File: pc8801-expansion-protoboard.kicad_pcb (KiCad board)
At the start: 2 copper layers, 219 x 95 mm, 11 parts, among them J1 Solder Side, J2 Parts Side, J3 5V, J4 12V, J5 -12V, J6 GND_1, J7 GND_2, U1 ExpansionEdge

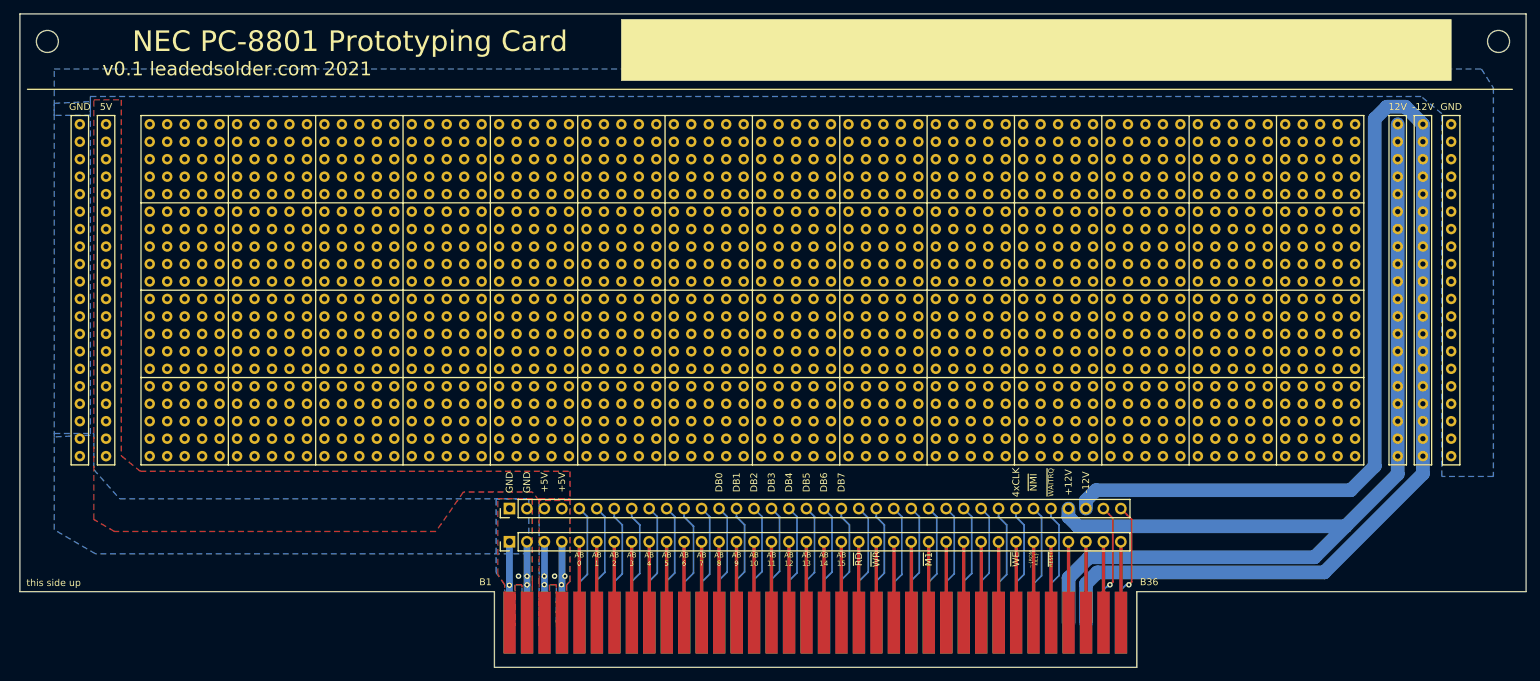
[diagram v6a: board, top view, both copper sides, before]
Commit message: ejector holes
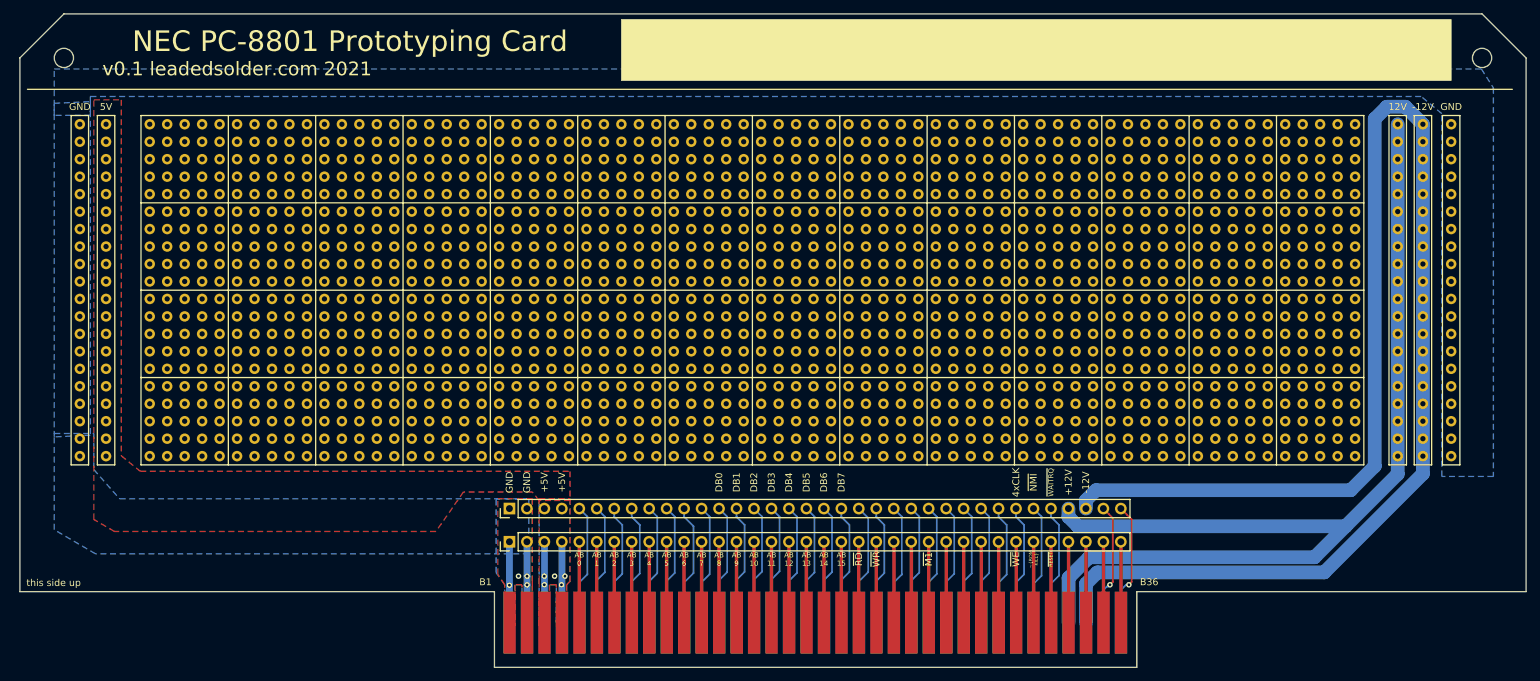
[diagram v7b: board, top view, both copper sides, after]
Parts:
- removed the REF** at (41.0, 54.0)
- removed the REF** at (252.0, 54.0)
- added REF**: MountingHole_2.7mm, MountingHole:MountingHole_2.7mm, F.Cu at (249.6, 56.4)
- added REF**: MountingHole_2.7mm, MountingHole:MountingHole_2.7mm, F.Cu at (43.4, 56.4)
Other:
- outline, holes or cut-outs redrawn
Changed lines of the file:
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@@
   (general
     (thickness 1.6)
-    (drawings 65)
+    (drawings 67)
     (tracks 245)
     (zones 0)
@@
     (38 B.Mask user)
     (39 F.Mask user)
-    (40 Dwgs.User user)
+    (40 Dwgs.User user hide)
     (41 Cmts.User user)
     (42 Eco1.User user)
@@
     (mod_text_size 1 1)
     (mod_text_width 0.15)
-    (pad_size 1.524 1.524)
-    (pad_drill 0.762)
+    (pad_size 2.8 2.8)
+    (pad_drill 2.8)
     (pad_to_mask_clearance 0.051)
     (solder_mask_min_width 0.25)
@@
     (add_net "Net-(J2-Pad9)")
   )
-  (module MountingHole:MountingHole_3.2mm_M3 locked (layer F.Cu)
-    (at 41 54)
-    (descr "Mounting Hole 3.2mm, no annular, M3")
-    (tags "mounting hole 3.2mm no annular m3")
+  (module MountingHole:MountingHole_2.7mm (layer F.Cu)
+    (at 249.6 56.4)
+    (descr "Mounting Hole 2.7mm, no annular")
+    (tags "mounting hole 2.7mm no annular")
     (attr virtual)
-    (fp_text reference REF** (at 0 -4.2) (layer F.SilkS) hide
-      (effects (font (size 1 1) (thickness 0.15)))
-    )
-    (fp_text value MountingHole_3.2mm_M3 (at 0 4.2) (layer F.Fab)
-      (effects (font (size 1 1) (thickness 0.15)))
-    )
-    (fp_circle (center 0 0) (end 3.45 0) (layer F.CrtYd) (width 0.05))
-    (fp_circle (center 0 0) (end 3.2 0) (layer Cmts.User) (width 0.15))
+    (fp_text reference REF** (at 0 -3.7) (layer F.SilkS) hide
+      (effects (font (size 1 1) (thickness 0.15)))
+    )
+    (fp_text value MountingHole_2.7mm (at 0 3.7) (layer F.Fab)
+      (effects (font (size 1 1) (thickness 0.15)))
+    )
+    (fp_circle (center 0 0) (end 2.95 0) (layer F.CrtYd) (width 0.05))
+    (fp_circle (center 0 0) (end 2.7 0) (layer Cmts.User) (width 0.15))
     (fp_text user %R (at 0.3 0) (layer F.Fab)
       (effects (font (size 1 1) (thickness 0.15)))
     )
-    (pad 1 np_thru_hole circle (at 0 0) (size 3.2 3.2) (drill 3.2) (layers *.Cu *.Mask))
-  )
-  (module MountingHole:MountingHole_3.2mm_M3 locked (layer F.Cu)
-    (at 252 54)
-    (descr "Mounting Hole 3.2mm, no annular, M3")
-    (tags "mounting hole 3.2mm no annular m3")
+    (pad "" np_thru_hole circle (at 0 0) (size 2.8 2.8) (drill 2.8) (layers *.Cu *.Mask))
+  )
+  (module MountingHole:MountingHole_2.7mm (layer F.Cu)
+    (at 43.4 56.4)
+    (descr "Mounting Hole 2.7mm, no annular")
+    (tags "mounting hole 2.7mm no annular")
     (attr virtual)
-    (fp_text reference REF** (at 0 -4.2) (layer F.SilkS) hide
-      (effects (font (size 1 1) (thickness 0.15)))
-    )
-    (fp_text value MountingHole_3.2mm_M3 (at 0 4.2) (layer F.Fab)
-      (effects (font (size 1 1) (thickness 0.15)))
-    )
-    (fp_circle (center 0 0) (end 3.45 0) (layer F.CrtYd) (width 0.05))
-    (fp_circle (center 0 0) (end 3.2 0) (layer Cmts.User) (width 0.15))
-    (fp_text user %R (at 0.3 0) (layer F.Fab)
-      (effects (font (size 1 1) (thickness 0.15)))
-    )
-    (pad 1 np_thru_hole circle (at 0 0) (size 3.2 3.2) (drill 3.2) (layers *.Cu *.Mask))
+    (fp_text reference REF** (at 0 -3.7) (layer F.SilkS) hide
+      (effects (font (size 1 1) (thickness 0.15)))
+    )
+    (fp_text value MountingHole_2.7mm (at 0 3.7) (layer F.Fab)
+      (effects (font (size 1 1) (thickness 0.15)))
+    )
+    (fp_circle (center 0 0) (end 2.95 0) (layer F.CrtYd) (width 0.05))
+    (fp_circle (center 0 0) (end 2.7 0) (layer Cmts.User) (width 0.15))
+    (fp_text user %R (at 0.3 0) (layer F.Fab) hide
+      (effects (font (size 1 1) (thickness 0.15)))
+    )
+    (pad "" np_thru_hole circle (at 0 0) (size 2.8 2.8) (drill 2.8) (layers *.Cu *.Mask))
   )
   (module "PC-8801:PC88 Edge" (layer F.Cu)
@@
     )
   )
+  (gr_line (start 256 56.4) (end 256 134) (layer Edge.Cuts) (width 0.05))
+  (gr_line (start 249.6 50) (end 43.4 50) (layer Edge.Cuts) (width 0.05))
+  (gr_line (start 249.6 50) (end 256 56.4) (layer Edge.Cuts) (width 0.05))
+  (dimension 6.4 (width 0.15) (layer Dwgs.User)
+    (gr_text "6.400 mm" (at 242.8 53.2 270) (layer Dwgs.User)
+      (effects (font (size 1 1) (thickness 0.15)))
+    )
+    (feature1 (pts (xy 256 56.4) (xy 243.513579 56.4)))
+    (feature2 (pts (xy 256 50) (xy 243.513579 50)))
+    (crossbar (pts (xy 244.1 50) (xy 244.1 56.4)))
+    (arrow1a (pts (xy 244.1 56.4) (xy 243.513579 55.273496)))
+    (arrow1b (pts (xy 244.1 56.4) (xy 244.686421 55.273496)))
+    (arrow2a (pts (xy 244.1 50) (xy 243.513579 51.126504)))
+    (arrow2b (pts (xy 244.1 50) (xy 244.686421 51.126504)))
+  )
+  (dimension 6.4 (width 0.15) (layer Dwgs.User)
+    (gr_text "6.400 mm" (at 252.8 61) (layer Dwgs.User)
+      (effects (font (size 1 1) (thickness 0.15)))
+    )
+    (feature1 (pts (xy 249.6 50) (xy 249.6 60.286421)))
+    (feature2 (pts (xy 256 50) (xy 256 60.286421)))
+    (crossbar (pts (xy 256 59.7) (xy 249.6 59.7)))
+    (arrow1a (pts (xy 249.6 59.7) (xy 250.726504 59.113579)))
+    (arrow1b (pts (xy 249.6 59.7) (xy 250.726504 60.286421)))
+    (arrow2a (pts (xy 256 59.7) (xy 254.873496 59.113579)))
+    (arrow2b (pts (xy 256 59.7) (xy 254.873496 60.286421)))
+  )
+  (gr_line (start 37 56.4) (end 37 134) (layer Edge.Cuts) (width 0.05))
+  (gr_line (start 43.4 50) (end 37 56.4) (layer Edge.Cuts) (width 0.05))
+  (dimension 6.4 (width 0.15) (layer Dwgs.User)
+    (gr_text "6.400 mm" (at 48.6 53.2 270) (layer Dwgs.User)
+      (effects (font (size 1 1) (thickness 0.15)))
+    )
+    (feature1 (pts (xy 37 56.4) (xy 47.886421 56.4)))
+    (feature2 (pts (xy 37 50) (xy 47.886421 50)))
+    (crossbar (pts (xy 47.3 50) (xy 47.3 56.4)))
+    (arrow1a (pts (xy 47.3 56.4) (xy 46.713579 55.273496)))
+    (arrow1b (pts (xy 47.3 56.4) (xy 47.886421 55.273496)))
+    (arrow2a (pts (xy 47.3 50) (xy 46.713579 51.126504)))
+    (arrow2b (pts (xy 47.3 50) (xy 47.886421 51.126504)))
+  )
+  (dimension 6.4 (width 0.15) (layer Dwgs.User)
+    (gr_text "6.400 mm" (at 40.2 58.7) (layer Dwgs.User)
+      (effects (font (size 1 1) (thickness 0.15)))
+    )
+    (feature1 (pts (xy 43.4 50) (xy 43.4 57.986421)))
+    (feature2 (pts (xy 37 50) (xy 37 57.986421)))
+    (crossbar (pts (xy 37 57.4) (xy 43.4 57.4)))
+    (arrow1a (pts (xy 43.4 57.4) (xy 42.273496 57.986421)))
+    (arrow1b (pts (xy 43.4 57.4) (xy 42.273496 56.813579)))
+    (arrow2a (pts (xy 37 57.4) (xy 38.126504 57.986421)))
+    (arrow2b (pts (xy 37 57.4) (xy 38.126504 56.813579)))
+  )
   (gr_text "nice soldering, keep it up" (at 245.75 133) (layer B.SilkS)
     (effects (font (size 1 1) (thickness 0.15)) (justify mirror))
@@
   (gr_line (start 199.4 134) (end 199.4 145) (layer Edge.Cuts) (width 0.05))
   (gr_line (start 256 134) (end 199.4 134) (layer Edge.Cuts) (width 0.05))
-  (dimension 7.5 (width 0.15) (layer Dwgs.User)
-    (gr_text "7.500 mm" (at 49.7 53.75 270) (layer Dwgs.User)
-      (effects (font (size 1 1) (thickness 0.15)))
-    )
-    (feature1 (pts (xy 37 57.5) (xy 48.986421 57.5)))
-    (feature2 (pts (xy 37 50) (xy 48.986421 50)))
-    (crossbar (pts (xy 48.4 50) (xy 48.4 57.5)))
-    (arrow1a (pts (xy 48.4 57.5) (xy 47.813579 56.373496)))
-    (arrow1b (pts (xy 48.4 57.5) (xy 48.986421 56.373496)))
-    (arrow2a (pts (xy 48.4 50) (xy 47.813579 51.126504)))
-    (arrow2b (pts (xy 48.4 50) (xy 48.986421 51.126504)))
-  )
-  (dimension 7.5 (width 0.15) (layer Dwgs.User)
-    (gr_text "7.500 mm" (at 40.75 62.8) (layer Dwgs.User)
-      (effects (font (size 1 1) (thickness 0.15)))
-    )
-    (feature1 (pts (xy 44.5 50) (xy 44.5 62.086421)))
-    (feature2 (pts (xy 37 50) (xy 37 62.086421)))
-    (crossbar (pts (xy 37 61.5) (xy 44.5 61.5)))
-    (arrow1a (pts (xy 44.5 61.5) (xy 43.373496 62.086421)))
-    (arrow1b (pts (xy 44.5 61.5) (xy 43.373496 60.913579)))
-    (arrow2a (pts (xy 37 61.5) (xy 38.126504 62.086421)))
-    (arrow2b (pts (xy 37 61.5) (xy 38.126504 60.913579)))
-  )
-  (dimension 7.5 (width 0.15) (layer Dwgs.User)
-    (gr_text "7.500 mm" (at 237.4 53.75 270) (layer Dwgs.User)
-      (effects (font (size 1 1) (thickness 0.15)))
-    )
-    (feature1 (pts (xy 256 57.5) (xy 238.113579 57.5)))
-    (feature2 (pts (xy 256 50) (xy 238.113579 50)))
-    (crossbar (pts (xy 238.7 50) (xy 238.7 57.5)))
-    (arrow1a (pts (xy 238.7 57.5) (xy 238.113579 56.373496)))
-    (arrow1b (pts (xy 238.7 57.5) (xy 239.286421 56.373496)))
-    (arrow2a (pts (xy 238.7 50) (xy 238.113579 51.126504)))
-    (arrow2b (pts (xy 238.7 50) (xy 239.286421 51.126504)))
-  )
-  (dimension 7.5 (width 0.15) (layer Dwgs.User)
-    (gr_text "7.500 mm" (at 252.25 40.5) (layer Dwgs.User)
-      (effects (font (size 1 1) (thickness 0.15)))
-    )
-    (feature1 (pts (xy 248.5 53.7) (xy 248.5 41.213579)))
-    (feature2 (pts (xy 256 53.7) (xy 256 41.213579)))
-    (crossbar (pts (xy 256 41.8) (xy 248.5 41.8)))
-    (arrow1a (pts (xy 248.5 41.8) (xy 249.626504 41.213579)))
-    (arrow1b (pts (xy 248.5 41.8) (xy 249.626504 42.386421)))
-    (arrow2a (pts (xy 256 41.8) (xy 254.873496 41.213579)))
-    (arrow2b (pts (xy 256 41.8) (xy 254.873496 42.386421)))
-  )
   (gr_poly (pts (xy 245.11 59.69) (xy 124.46 59.69) (xy 124.46 50.8) (xy 245.11 50.8)) (layer F.SilkS) (width 0.1))
   (gr_line (start 254 60.96) (end 38.1 60.96) (layer F.SilkS) (width 0.12))
@@
     (effects (font (size 1 1) (thickness 0.15)))
   )
-  (gr_line (start 37 134) (end 37 50) (layer Edge.Cuts) (width 0.05))
-  (gr_line (start 256 50) (end 256 134) (layer Edge.Cuts) (width 0.05))
-  (gr_line (start 37 50) (end 256 50) (layer Edge.Cuts) (width 0.05))
   (segment (start 197.1 126.766) (end 197.08 126.746) (width 0.5) (layer F.Cu) (net 1))
   (segment (start 197.1 138.5) (end 197.1 126.766) (width 0.5) (layer F.Cu) (net 1))
